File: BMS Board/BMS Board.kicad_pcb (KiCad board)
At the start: 2 copper layers, 192 parts, among them U1 BQ76920PW, U2 TCA9548APWR, U3 BQ76920PW, U4 BQ76920PW, U5 BQ76920PW, U6 BQ76920PW, U7 BQ76920PW, U8 BQ76920PW, U9 BQ76930DBT

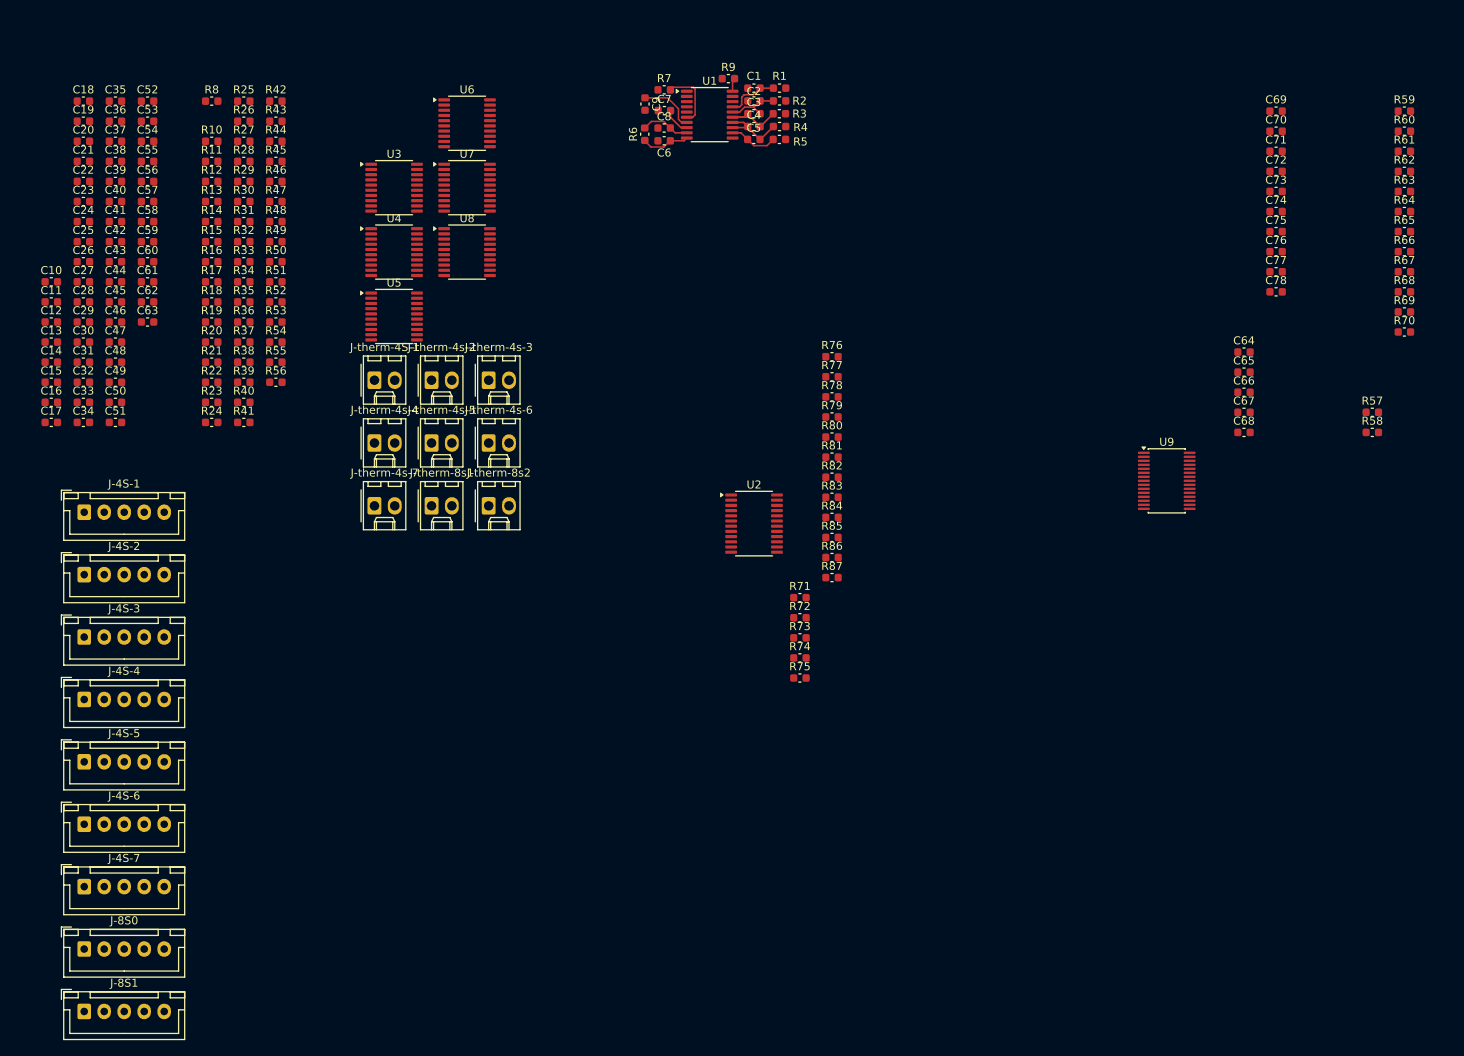
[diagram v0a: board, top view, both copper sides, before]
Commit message: BMS layout for three batteries done
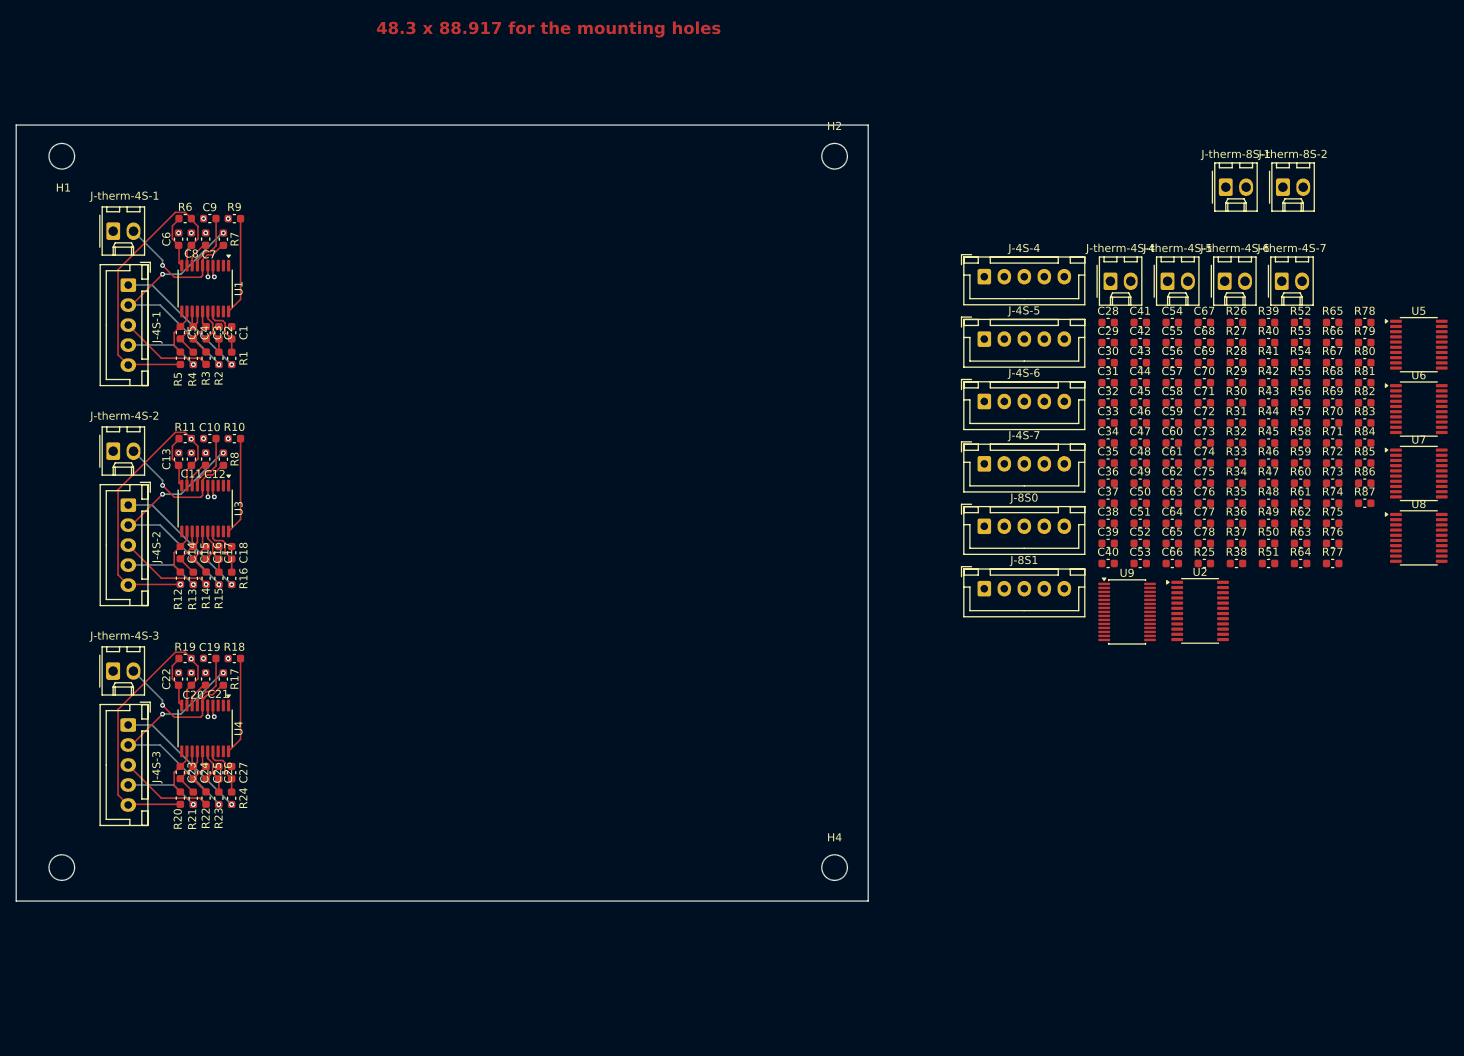
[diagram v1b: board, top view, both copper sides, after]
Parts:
- removed J-therm-4s-2, J-therm-4s-3, J-therm-4s-4, J-therm-4s-5, J-therm-4s-6, J-therm-4s-7, J-therm-8s1, J-therm-8s2: Conn_01x02, Connector_Molex:Molex_KK-254_AE-6410-02A_1x02_P2.54mm_Vertical
- added H1: MountingHole, MountingHole:MountingHole_3.2mm_M3_DIN965, F.Cu at (26.2, 33.9)
- added H2: MountingHole, MountingHole:MountingHole_3.2mm_M3_DIN965, F.Cu at (122.8, 33.9)
- added H3: MountingHole, MountingHole:MountingHole_3.2mm_M3_DIN965, F.Cu at (26.2, 122.8)
- added H4: MountingHole, MountingHole:MountingHole_3.2mm_M3_DIN965, F.Cu at (122.8, 122.8)
- added J-therm-4S-2: Conn_01x02, Connector_Molex:Molex_KK-254_AE-6410-02A_1x02_P2.54mm_Vertical, F.Cu at (32.6, 70.8)
- added J-therm-4S-3: Conn_01x02, Connector_Molex:Molex_KK-254_AE-6410-02A_1x02_P2.54mm_Vertical, F.Cu at (32.6, 98.3)
- added J-therm-4S-4: Conn_01x02, Connector_Molex:Molex_KK-254_AE-6410-02A_1x02_P2.54mm_Vertical, F.Cu at (157.3, 49.5)
- added J-therm-4S-5: Conn_01x02, Connector_Molex:Molex_KK-254_AE-6410-02A_1x02_P2.54mm_Vertical, F.Cu at (164.4, 49.5)
- added J-therm-4S-6: Conn_01x02, Connector_Molex:Molex_KK-254_AE-6410-02A_1x02_P2.54mm_Vertical, F.Cu at (171.6, 49.5)
- added J-therm-4S-7: Conn_01x02, Connector_Molex:Molex_KK-254_AE-6410-02A_1x02_P2.54mm_Vertical, F.Cu at (178.7, 49.5)
- added J-therm-8S-1: Conn_01x02, Connector_Molex:Molex_KK-254_AE-6410-02A_1x02_P2.54mm_Vertical, F.Cu at (171.7, 37.8)
- added J-therm-8S-2: Conn_01x02, Connector_Molex:Molex_KK-254_AE-6410-02A_1x02_P2.54mm_Vertical, F.Cu at (178.8, 37.8)
- moved C52 135.8 mm to (161.0, 82.3)
- moved C53 135.8 mm to (161.0, 84.8)
- moved R25 133.3 mm to (169.0, 84.8)
- moved C35 132.1 mm to (157.0, 72.3)
- moved C36 132.1 mm to (157.0, 74.8)
- moved C37 132.1 mm to (157.0, 77.3)
- moved C38 132.1 mm to (157.0, 79.8)
- moved C39 132.1 mm to (157.0, 82.3)
- moved C40 132.1 mm to (157.0, 84.8)
- moved C54 130.1 mm to (165.0, 54.7)
- moved C55 130.1 mm to (165.0, 57.2)
- moved C56 130.1 mm to (165.0, 59.7)
- moved C57 130.1 mm to (165.0, 62.2)
- moved C58 130.1 mm to (165.0, 64.7)
- moved C59 130.1 mm to (165.0, 67.2)
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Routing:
- net /4S3-VC4: track 0.00 -> 38.0 mm, vias 0 -> 1
- net /4S2-VC4: track 0.00 -> 38.0 mm, vias 0 -> 2
- net /4S1-VC4: track 6.19 -> 38.0 mm
- net /4S1-VC1: track 0.00 -> 30.1 mm, vias 0 -> 3
- net /4S3-VC1: track 0.00 -> 30.1 mm, vias 0 -> 3
- net /4S2-VC1: track 0.00 -> 30.1 mm, vias 0 -> 3
- net /THERM3: track 0.00 -> 17.4 mm, vias 0 -> 1
- net /4S3-VC0: track 0.00 -> 17.0 mm, vias 0 -> 1
- net /4S2-VC0: track 0.00 -> 17.0 mm, vias 0 -> 1
- net /4S1-VC0: track 0.00 -> 17.0 mm, vias 0 -> 1
- net /THERM2: track 0.00 -> 16.9 mm, vias 0 -> 1
- net /4S3-VC2: track 0.00 -> 12.8 mm
- net /4S1-VC2: track 0.00 -> 12.8 mm
- net /4S2-VC2: track 0.00 -> 12.8 mm, vias 0 -> 1
- net Net-(U4-ALERT): track 0.00 -> 12.2 mm
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- added copper zone on In1.Cu, net GND
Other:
- board outline added: 106.5 x 97 mm
- copper layers 2 -> 4
- board text added: "48.3 x 88.917 for the mounting holes"

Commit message: BMS pretty much completed
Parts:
- added C79: 1uF, Capacitor_SMD:C_0603_1608Metric, F.Cu at (105.9, 112.2)
- added C80: 1uF, Capacitor_SMD:C_0603_1608Metric, F.Cu at (109.5, 112.1)
- added D1: D, Diode_SMD:D_SOD-123, F.Cu at (99.8, 96.9)
- added D2: D, Diode_SMD:D_SOD-123, F.Cu at (100.6, 82.7)
- added J1: Conn_01x02, Connector_AMASS:AMASS_XT30UPB-F_1x02_P5.0mm_Vertical, F.Cu at (95.2, 115.0)
- added J_I2C1: Conn_02x02_Counter_Clockwise, Connector_Molex:Molex_Nano-Fit_105309-xx04_1x04_P2.50mm_Vertical, F.Cu at (120.1, 92.0)
- added Q1: NMOS, Package_TO_SOT_SMD:SOT-23, F.Cu at (90.3, 99.3)
- added U10: TLV70033_SOT23-5, Package_TO_SOT_SMD:SOT-23-5, F.Cu at (108.0, 116.2)
- moved U7 130.7 mm to (69.1, 105.4), turned to -90 degrees
- moved U6 127.3 mm to (69.1, 77.9), turned to -90 degrees
- moved U5 126.9 mm to (69.1, 50.4), turned to -90 degrees
- moved J-therm-4S-6 123.9 mm to (57.6, 98.3)
- moved J-therm-8S-2 121.3 mm to (82.8, 111.9)
- moved R44 120.5 mm to (66.0, 114.2), turned to -90 degrees
- moved R45 118.1 mm to (67.6, 114.2), turned to -90 degrees
- moved R46 115.7 mm to (69.2, 114.2), turned to -90 degrees
- moved R43 115.0 mm to (66.6, 96.7)
- moved R47 113.3 mm to (70.8, 114.2), turned to -90 degrees
- moved R41 112.8 mm to (71.4, 99.3), turned to -90 degrees
- moved R48 110.9 mm to (72.4, 114.2), turned to -90 degrees
- moved R39 110.9 mm to (70.8, 86.7), turned to -90 degrees
- moved R42 109.8 mm to (72.8, 96.7)
- moved J-therm-4S-5 108.9 mm to (57.6, 70.8)
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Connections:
- J-8S0 pad 1: unconnected-(J-8S0-Pin_1-Pad1) -> /8S-VC0
- J-8S0 pad 2: unconnected-(J-8S0-Pin_2-Pad2) -> /8S-VC1
- J-8S0 pad 3: unconnected-(J-8S0-Pin_3-Pad3) -> /8S-VC2
- J-8S0 pad 4: unconnected-(J-8S0-Pin_4-Pad4) -> /8S-VC3
- J-8S0 pad 5: unconnected-(J-8S0-Pin_5-Pad5) -> /8S-VC4
- J-8S1 pad 1: unconnected-(J-8S1-Pin_1-Pad1) -> /8S-VC4
- J-8S1 pad 2: unconnected-(J-8S1-Pin_2-Pad2) -> /8S-VC6
- J-8S1 pad 3: unconnected-(J-8S1-Pin_3-Pad3) -> /8S-VC7
- J-8S1 pad 4: unconnected-(J-8S1-Pin_4-Pad4) -> /8S-VC8
- J-8S1 pad 5: unconnected-(J-8S1-Pin_5-Pad5) -> /8S-VC9
- R71 pad 2: /SC0 -> /SC6
- R72 pad 2: /SD0 -> /SD6
- R73 pad 2: /SC1 -> /SC3
- R74 pad 2: /SD1 -> /SD3
- R75 pad 2: /SC2 -> /SC0
- R76 pad 2: /SD2 -> /SD0
- R77 pad 2: /SC3 -> /SC1
- R78 pad 2: /SD3 -> /SD1
- R81 pad 1: /SC5 -> /SC2
- R82 pad 1: /SD5 -> /SD2
- R83 pad 1: /SC6 -> /SC5
- R85 pad 1: /SD6 -> /SD5
- U2 pad 10: /SD3 -> /SD1
- U2 pad 11: /SC3 -> /SC1
- U2 pad 15: /SD5 -> /SD2
- U2 pad 16: /SC5 -> /SC2
- U2 pad 17: /SD6 -> /SD5
- U2 pad 18: /SC6 -> /SC5
- U2 pad 4: /SD0 -> /SD6
- U2 pad 5: /SC0 -> /SC6
- U2 pad 6: /SD1 -> /SD3
- U2 pad 7: /SC1 -> /SC3
- U2 pad 8: /SD2 -> /SD0
- U2 pad 9: /SC2 -> /SC0
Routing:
- net /SC2: track 1.47 -> 87.8 mm, vias 1 -> 2
- net /SD2: track 1.48 -> 86.0 mm, vias 1 -> 2
- net /SD0: track 1.48 -> 83.2 mm, vias 1 -> 2
- net /SC0: track 1.47 -> 81.8 mm, vias 1 -> 2
- net /SC1: track 1.47 -> 74.2 mm, vias 1 -> 2
- net /SD1: track 1.48 -> 73.6 mm, vias 1 -> 2
- net /SC5: track 0.00 -> 64.4 mm, vias 0 -> 2
- net /SD5: track 0.00 -> 62.7 mm, vias 0 -> 2
- net /SC3: track 0.00 -> 60.7 mm, vias 0 -> 2
- net /SD3: track 0.00 -> 58.3 mm, vias 0 -> 2
- net /SC4: track 0.00 -> 47.4 mm, vias 0 -> 2
- net /SD4: track 0.00 -> 43.4 mm, vias 0 -> 2
- net /SC7: track 0.00 -> 43.1 mm, vias 0 -> 2
- net /VC5X: track 0.00 -> 42.9 mm, vias 0 -> 2
- net /SD7: track 0.00 -> 42.4 mm, vias 0 -> 2
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- added copper zone on B.Cu, net /3.3V
- added copper zone on F.Cu, net /5V
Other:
- board text added: "BATT 1"
- board text added: "BATT 2"
- board text added: "BATT 3"
- board text added: "BATT 4"
- board text added: "BATT 5"
- board text added: "BATT 6"
- board text added: "BATT 7"
- board text added: "Battery Management System Board v1 - 05/26 Princeton Rover Team Aaryan Jagtap"
- board text removed: "48.3 x 88.917 for the mounting holes"

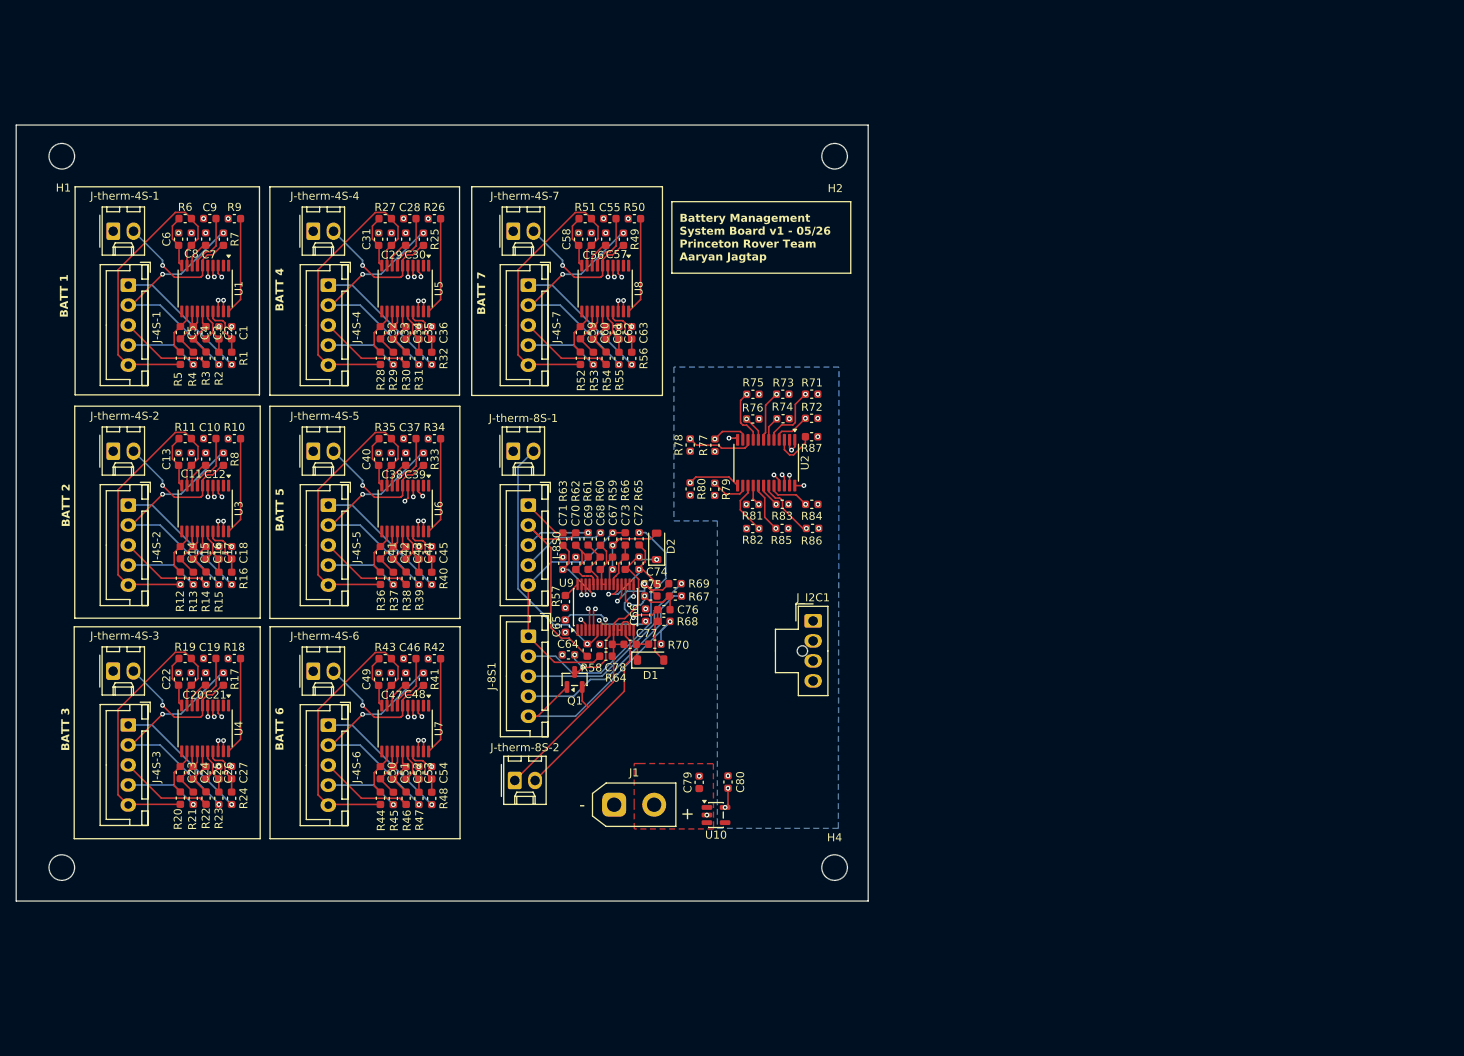
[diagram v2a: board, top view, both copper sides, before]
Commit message: BMS completed + via stitching
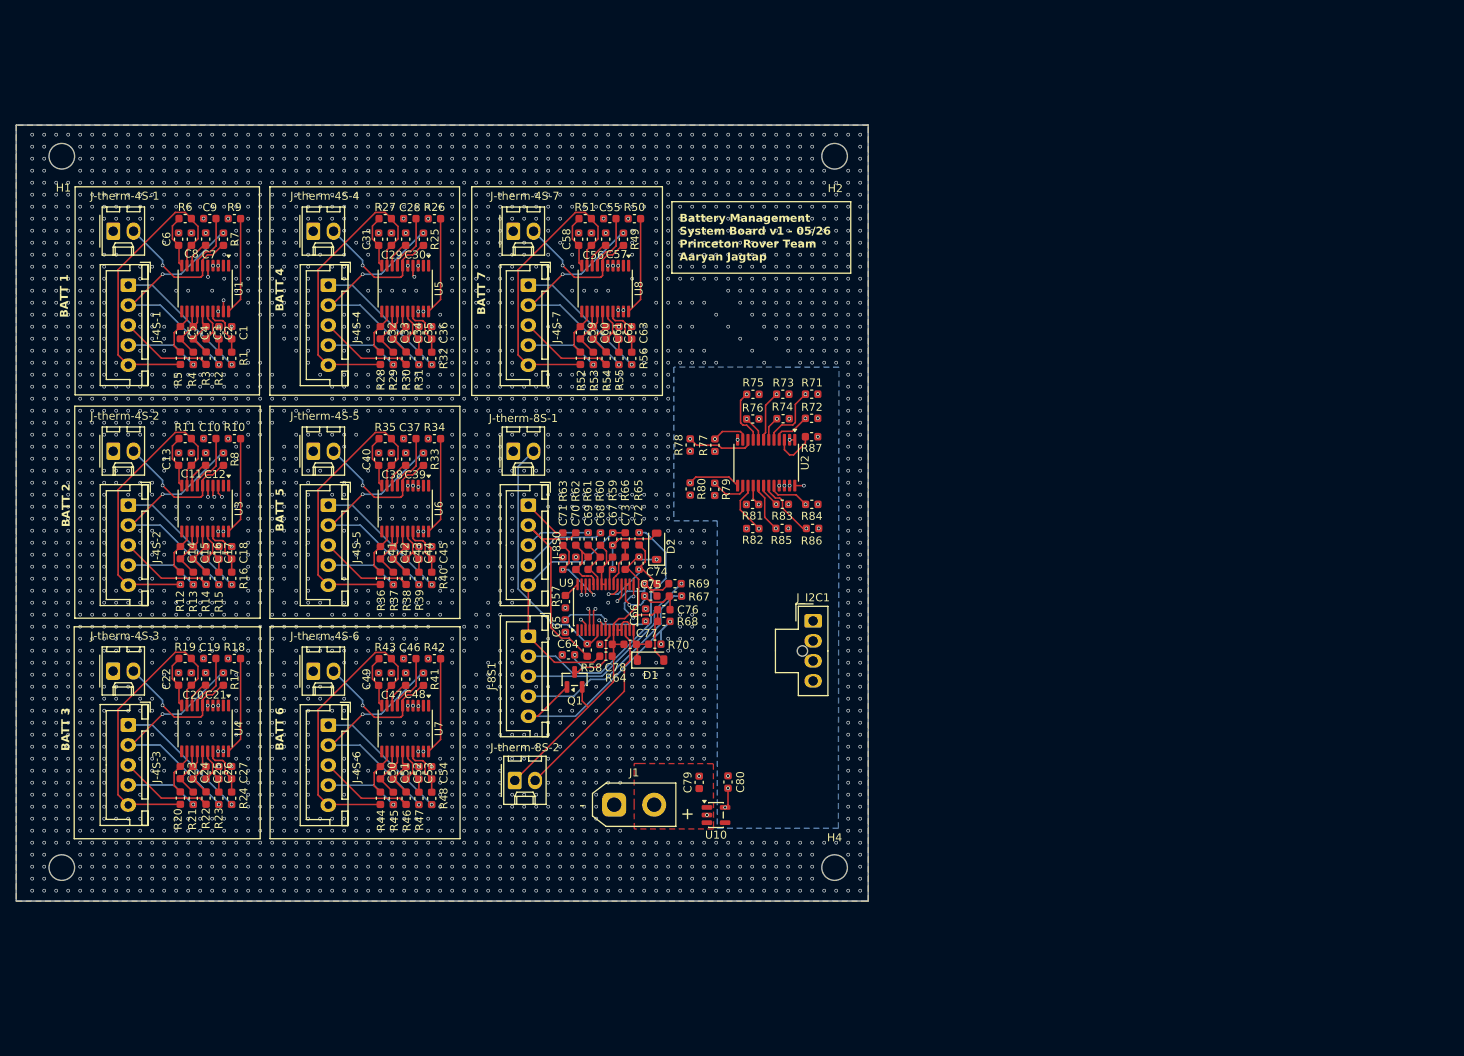
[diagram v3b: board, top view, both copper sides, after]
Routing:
- net GND: track 38.7 -> 9.14 mm, vias 86 -> 2825
- net /SDA: track 22.7 -> 19.5 mm
- net /SC2: track 87.8 -> 85.2 mm
- net /SCL: track 32.4 -> 30.4 mm
- net /SD4: track 43.4 -> 41.5 mm
- net /SD5: track 62.7 -> 61.0 mm
- net /SC4: track 47.4 -> 45.8 mm
- net /SD2: track 86.0 -> 84.6 mm
- net /SD0: track 83.2 -> 81.8 mm
- net /SC3: track 60.7 -> 59.4 mm
- net /SC5: track 64.4 -> 63.6 mm
- added copper zone on B.Cu, net GND
- added copper zone on F.Cu, net GND
- added copper zone on In2.Cu, net GND
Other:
- board text added: "${REFERENCE}"
- board text added: "{ "ViaStitching": "0.2", "stitch_zone_0": { "HSpacing": "1", "VSpacing": "1", "HOffset": "0", "VOffset": "0", "Clearance": "0", "Randomize": false } }"
